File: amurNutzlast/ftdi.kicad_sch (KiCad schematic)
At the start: 30 parts, among them J2 USB_A, U3 LD1117S33TR_SOT223, U4 FT2232HL, U5 93LCxxA, Y1 12MHz

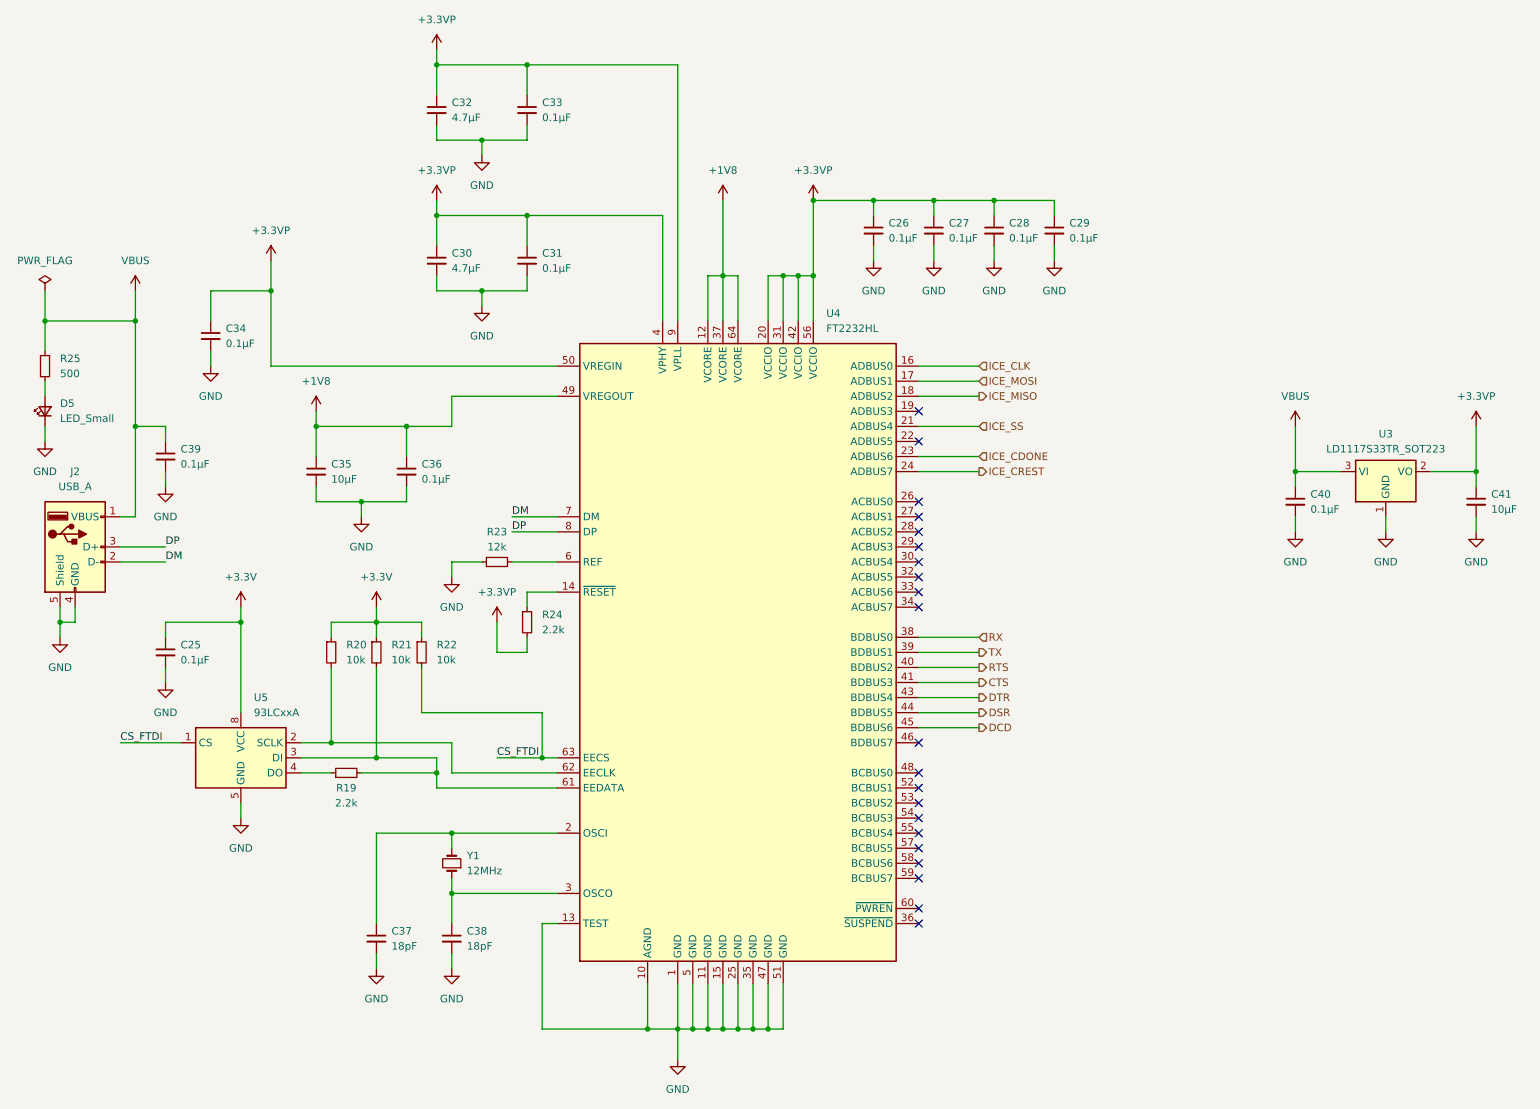
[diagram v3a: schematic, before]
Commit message: deleted 3.3 converter for ftdi and moved USB to a hierarhical sheet
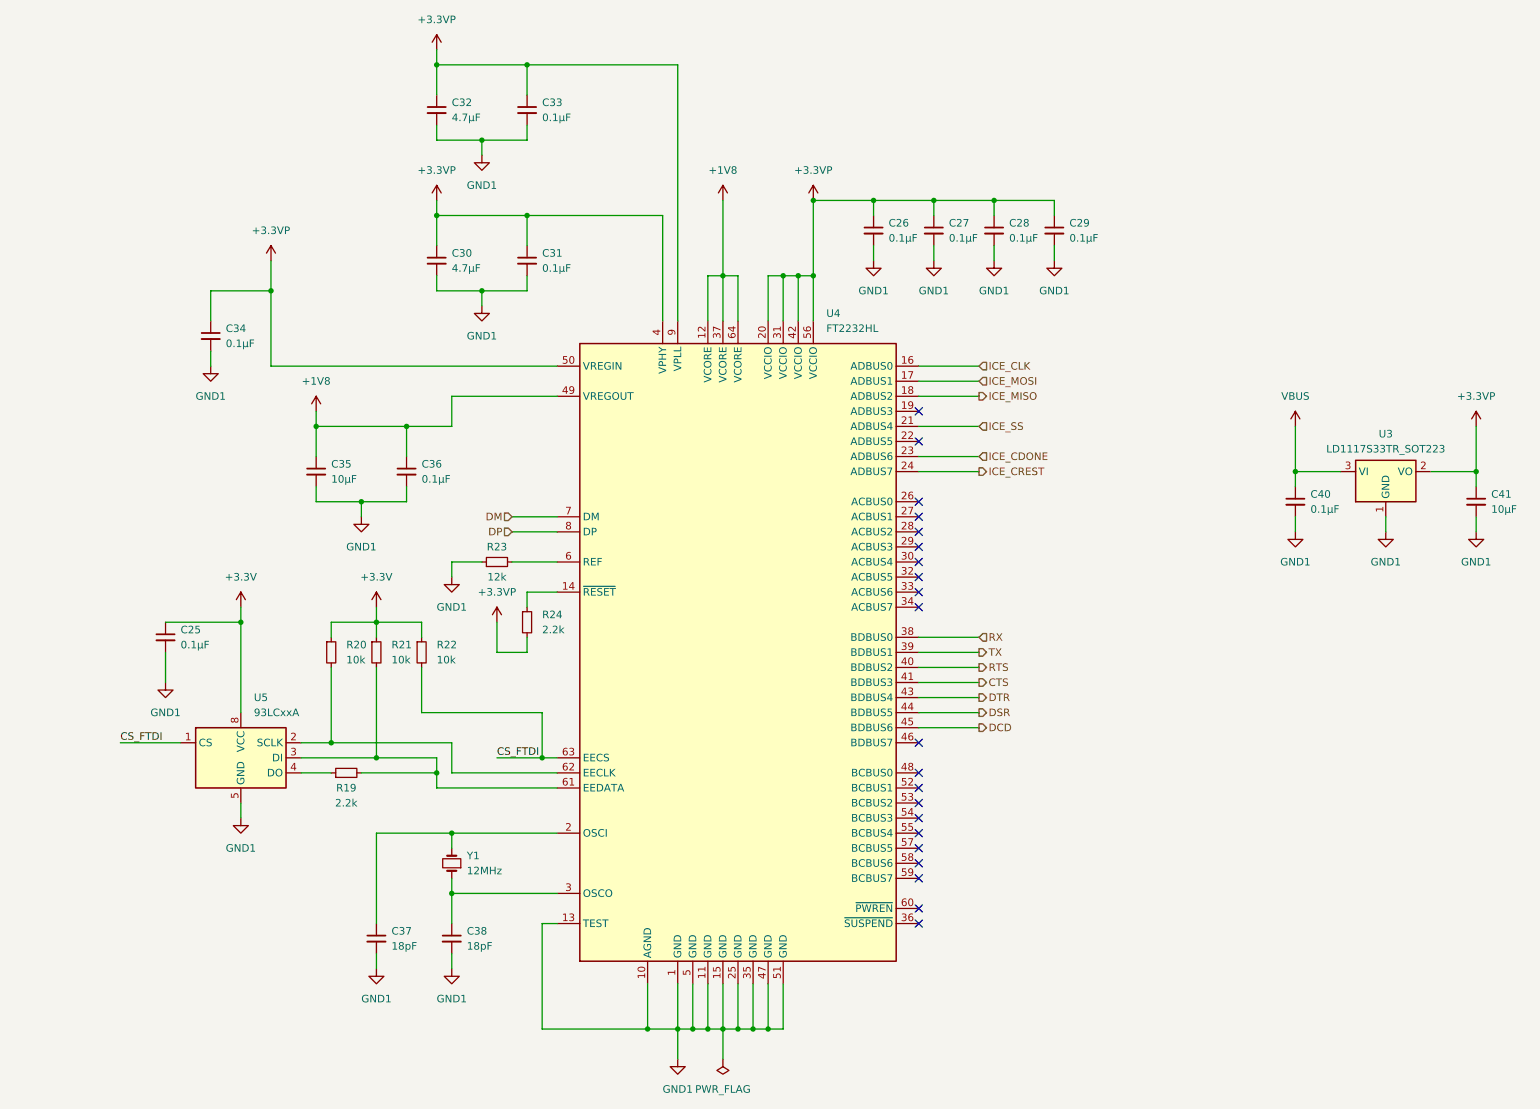
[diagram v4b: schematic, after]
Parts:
- removed C39: 0.1µF, Capacitor_SMD:C_0603_1608Metric, symbol Device:C_Small
- removed D5: LED_Small, LED_SMD:LED_0603_1608Metric, symbol Device:LED_Small
- removed J2: USB_A, Connector_USB:USB_A_CNCTech_1001-011-01101_Horizontal, symbol Connector:USB_A
- removed R25: 500, Resistor_SMD:R_0603_1608Metric, symbol Device:R_Small
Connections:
- net GND renamed GND1
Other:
- moved on the sheet: C25
